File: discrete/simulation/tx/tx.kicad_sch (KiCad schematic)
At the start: 0 parts

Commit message: Add and validate discrete DEC logic level converter simulation
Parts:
- added D1: 1N914, Diode_THT:D_DO-35_SOD27_P7.62mm_Horizontal, symbol Diode:1N914
- added Q1: 2N3904, Package_TO_SOT_THT:TO-92_Inline, symbol Transistor_BJT:2N3904
- added Q2: 2N3906, Package_TO_SOT_THT:TO-92_Inline, symbol Transistor_BJT:2N3906
- added R1: 27k, symbol Device:R
- added R2: 180k, symbol Device:R
- added R3, R5: 100k, symbol Device:R
- added R4: 33k, symbol Device:R
- added R6: 10k, symbol Device:R
- added V1: 10, symbol Simulation_SPICE:VDC
- added V2: 15, symbol Simulation_SPICE:VDC
- added V3: VPULSE, symbol Simulation_SPICE:VPULSE
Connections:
- new net: Q2.2 (B), R4.2, R5.2
- new net: D1.1 (K), Q1.2 (B), R1.2, R2.2
- new net +10V: Q2.1 (E), R2.1, R3.1, R5.1, V1.1
- new net -15V: R6.2, V2.2
- new net DRV: Q2.3 (C), R6.1
- new net GND: D1.2 (A), Q1.1 (E), V1.2, V2.1, V3.2
- new net Q1_C: Q1.3 (C), R3.2, R4.1
- new net TTO: R1.1, V3.1

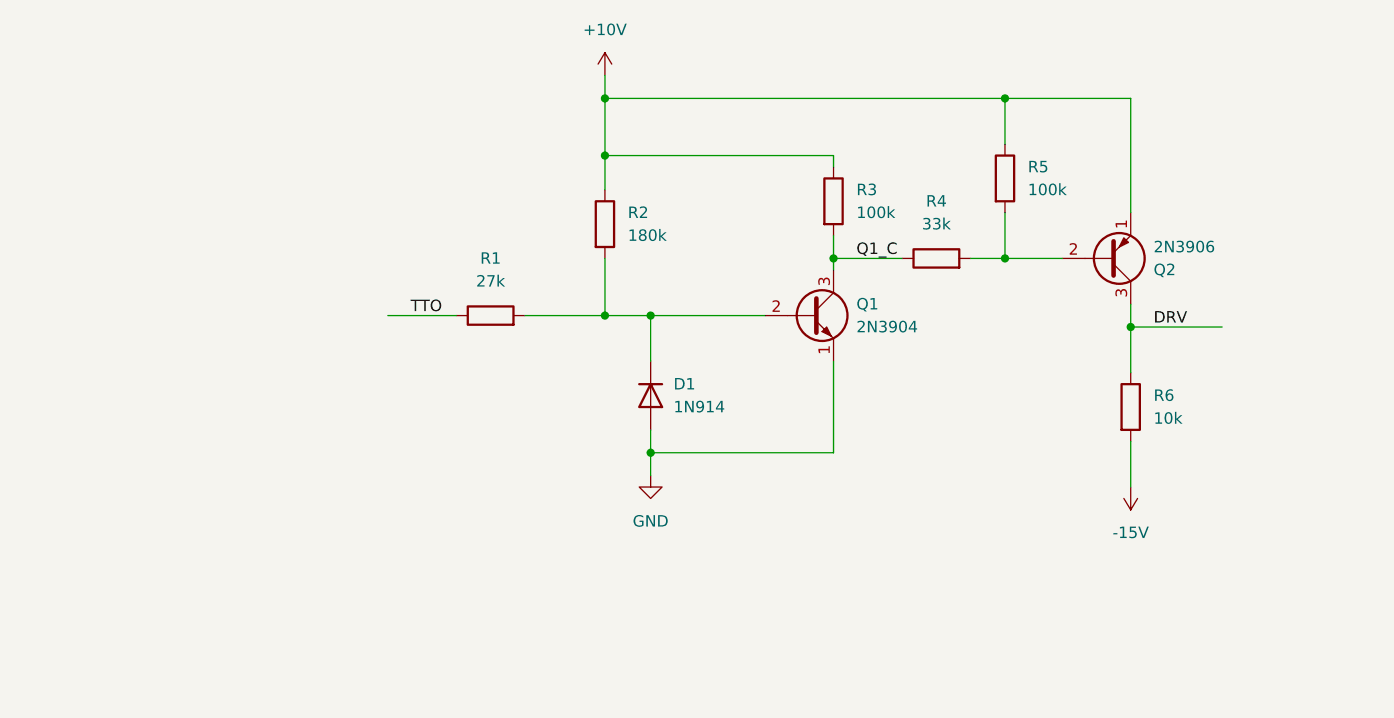
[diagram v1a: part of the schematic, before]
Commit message: Add and validate complementary RS232 transmitter output stage
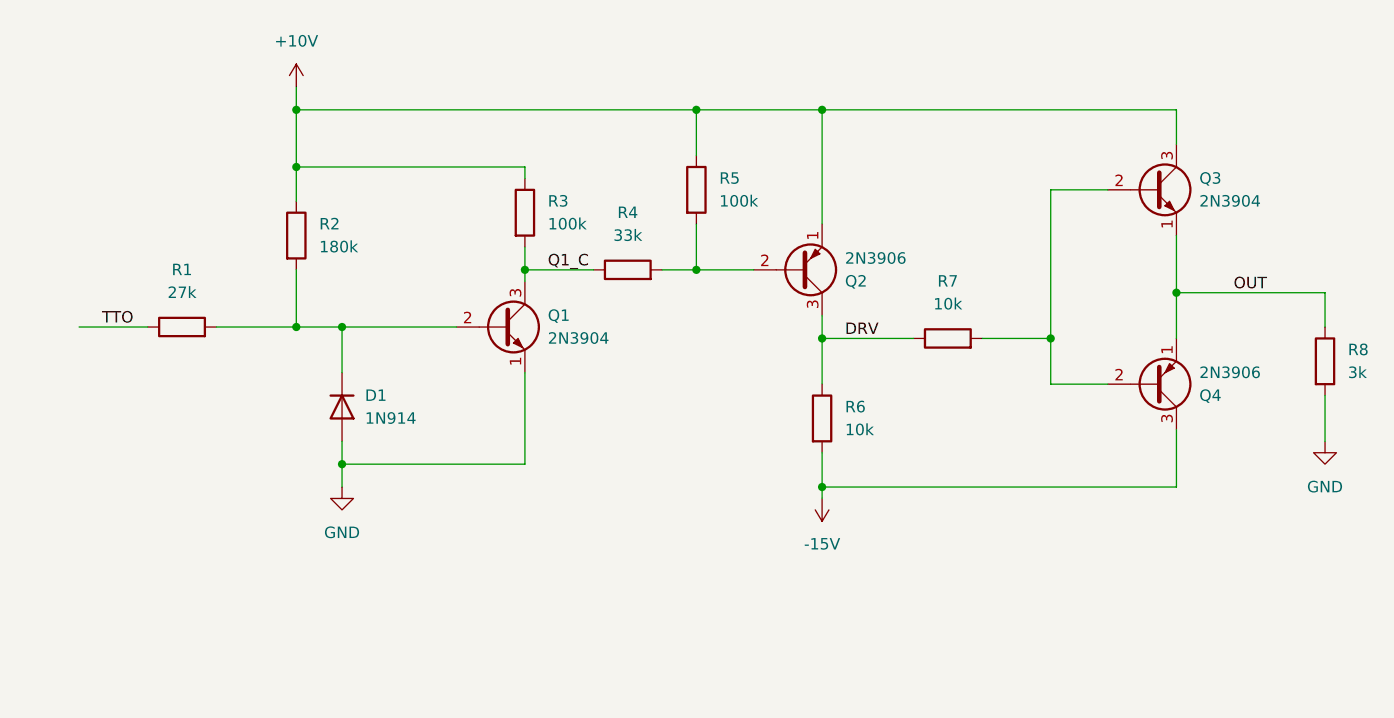
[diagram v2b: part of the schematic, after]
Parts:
- added Q3: 2N3904, Package_TO_SOT_THT:TO-92_Inline, symbol Transistor_BJT:2N3904
- added Q4: 2N3906, Package_TO_SOT_THT:TO-92_Inline, symbol Transistor_BJT:2N3906
- added R7: 10k, symbol Device:R
- added R8: 3k, symbol Device:R
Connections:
- net +10V: now also Q3.3 (C)
- net -15V: now also Q4.3 (C)
- net DRV: now also R7.1
- net GND: now also R8.2
- new net: Q3.2 (B), Q4.2 (B), R7.2
- new net OUT: Q3.1 (E), Q4.1 (E), R8.1
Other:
- moved on the sheet: D1, Q1, Q2, R1, R2, R3, R4, R5, R6

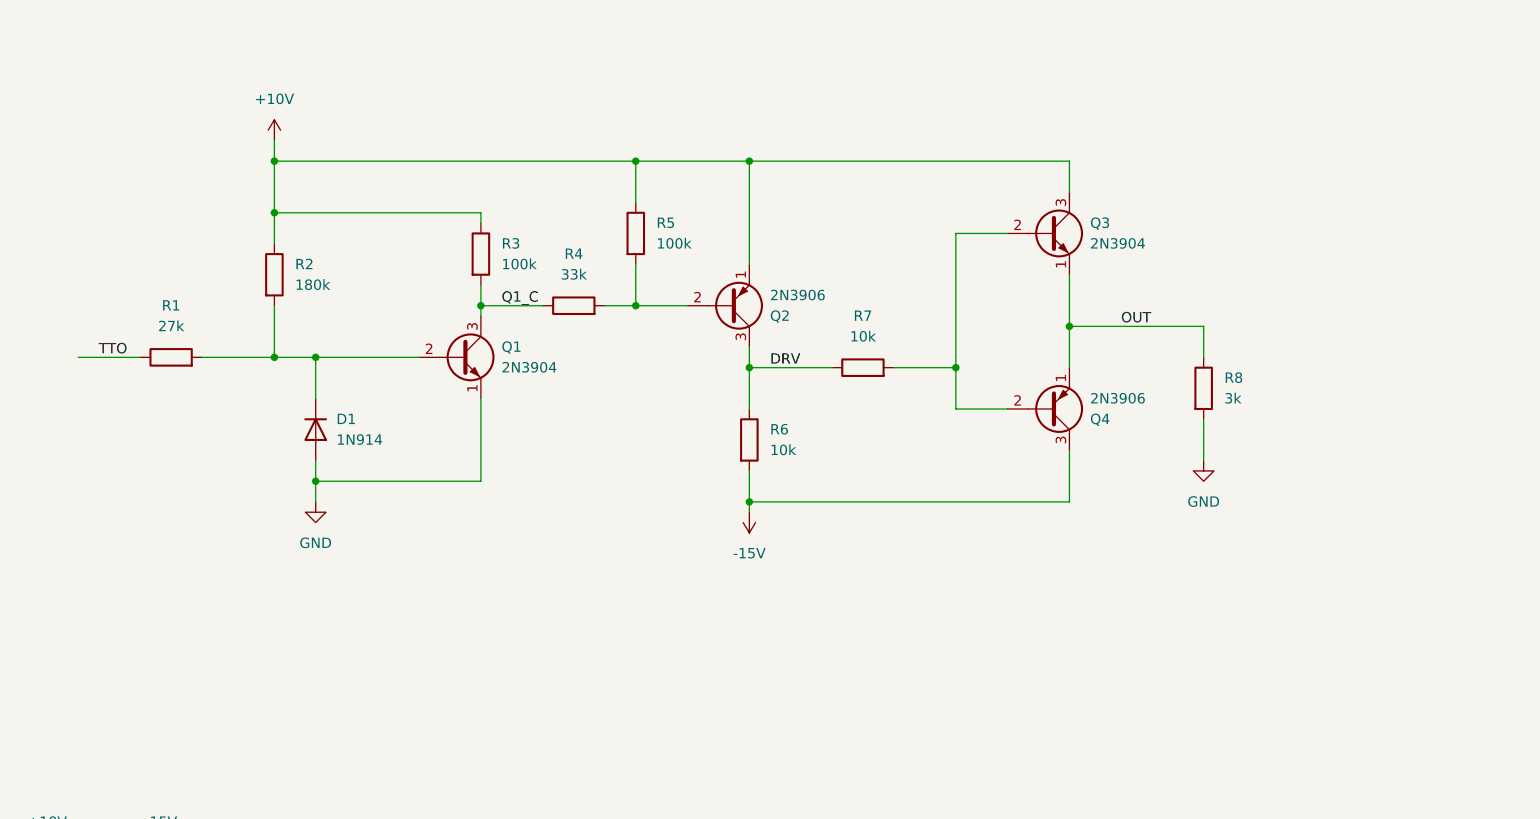
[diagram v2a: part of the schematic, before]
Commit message: Add RS232 transmitter normal load simulation
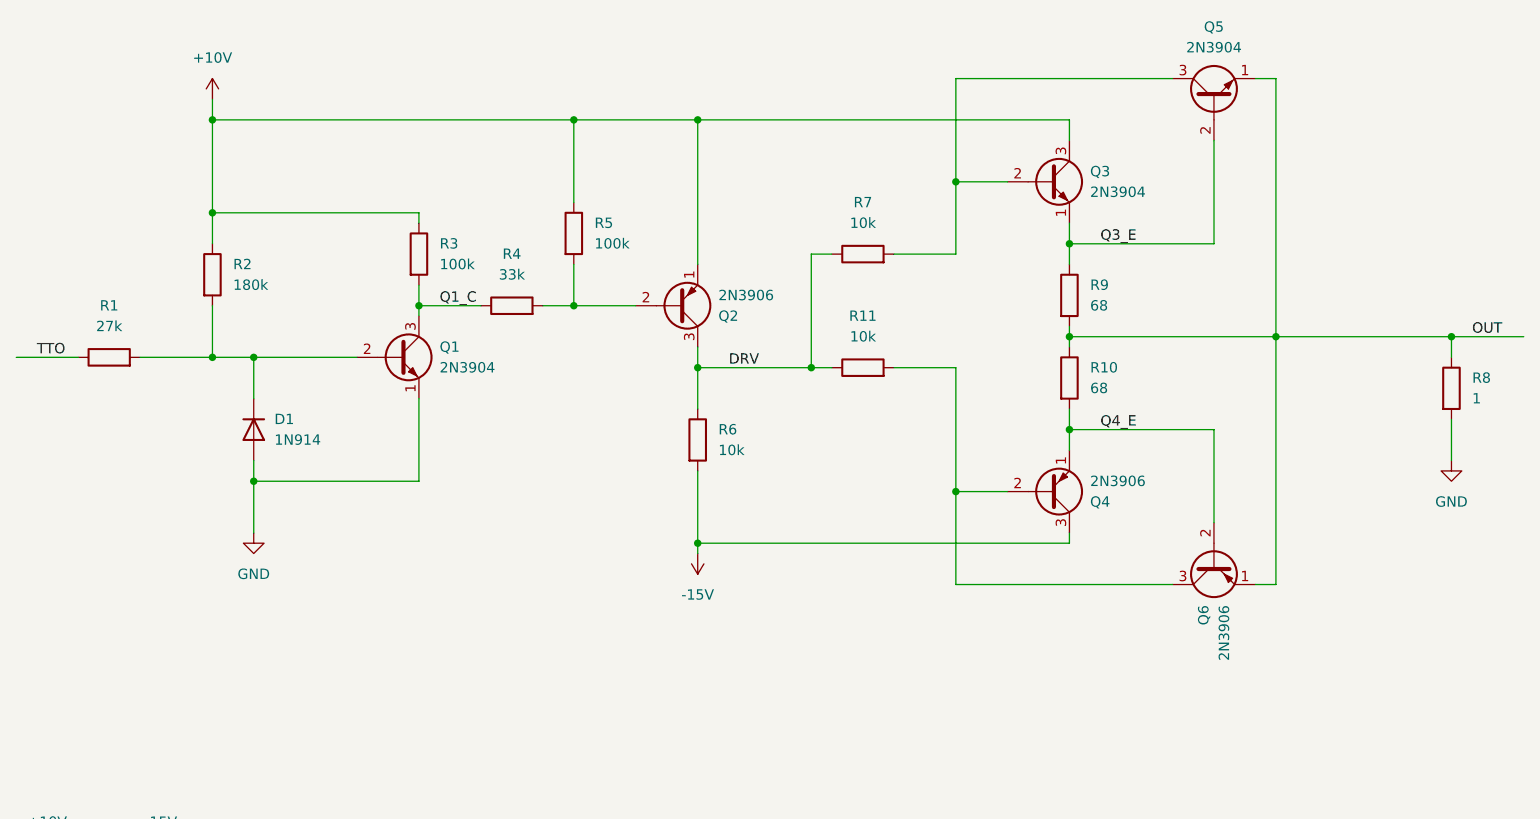
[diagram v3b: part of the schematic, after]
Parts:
- added Q5: 2N3904, Package_TO_SOT_THT:TO-92_Inline, symbol Transistor_BJT:2N3904
- added Q6: 2N3906, Package_TO_SOT_THT:TO-92_Inline, symbol Transistor_BJT:2N3906
- added R10, R9: 68, symbol Device:R
- added R7: 10k, symbol Device:R
- R8: value 3k -> 1
- renumbered R7 to R11
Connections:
- net DRV: now also R7.1
- net OUT: now also Q5.1 (E), Q6.1 (E), R10.1, R9.2; no longer Q3.1 (E), Q4.1 (E)
- net at Q4.2 (B), R11.2: now also Q6.3 (C); no longer Q3.2 (B)
- new net: Q3.2 (B), Q5.3 (C), R7.2
- new net Q3_E: Q3.1 (E), Q5.2 (B), R9.1
- new net Q4_E: Q4.1 (E), Q6.2 (B), R10.2
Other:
- moved on the sheet: D1, Q1, Q2, Q3, Q4, R1, R2, R3, R4, R5, R6, R8

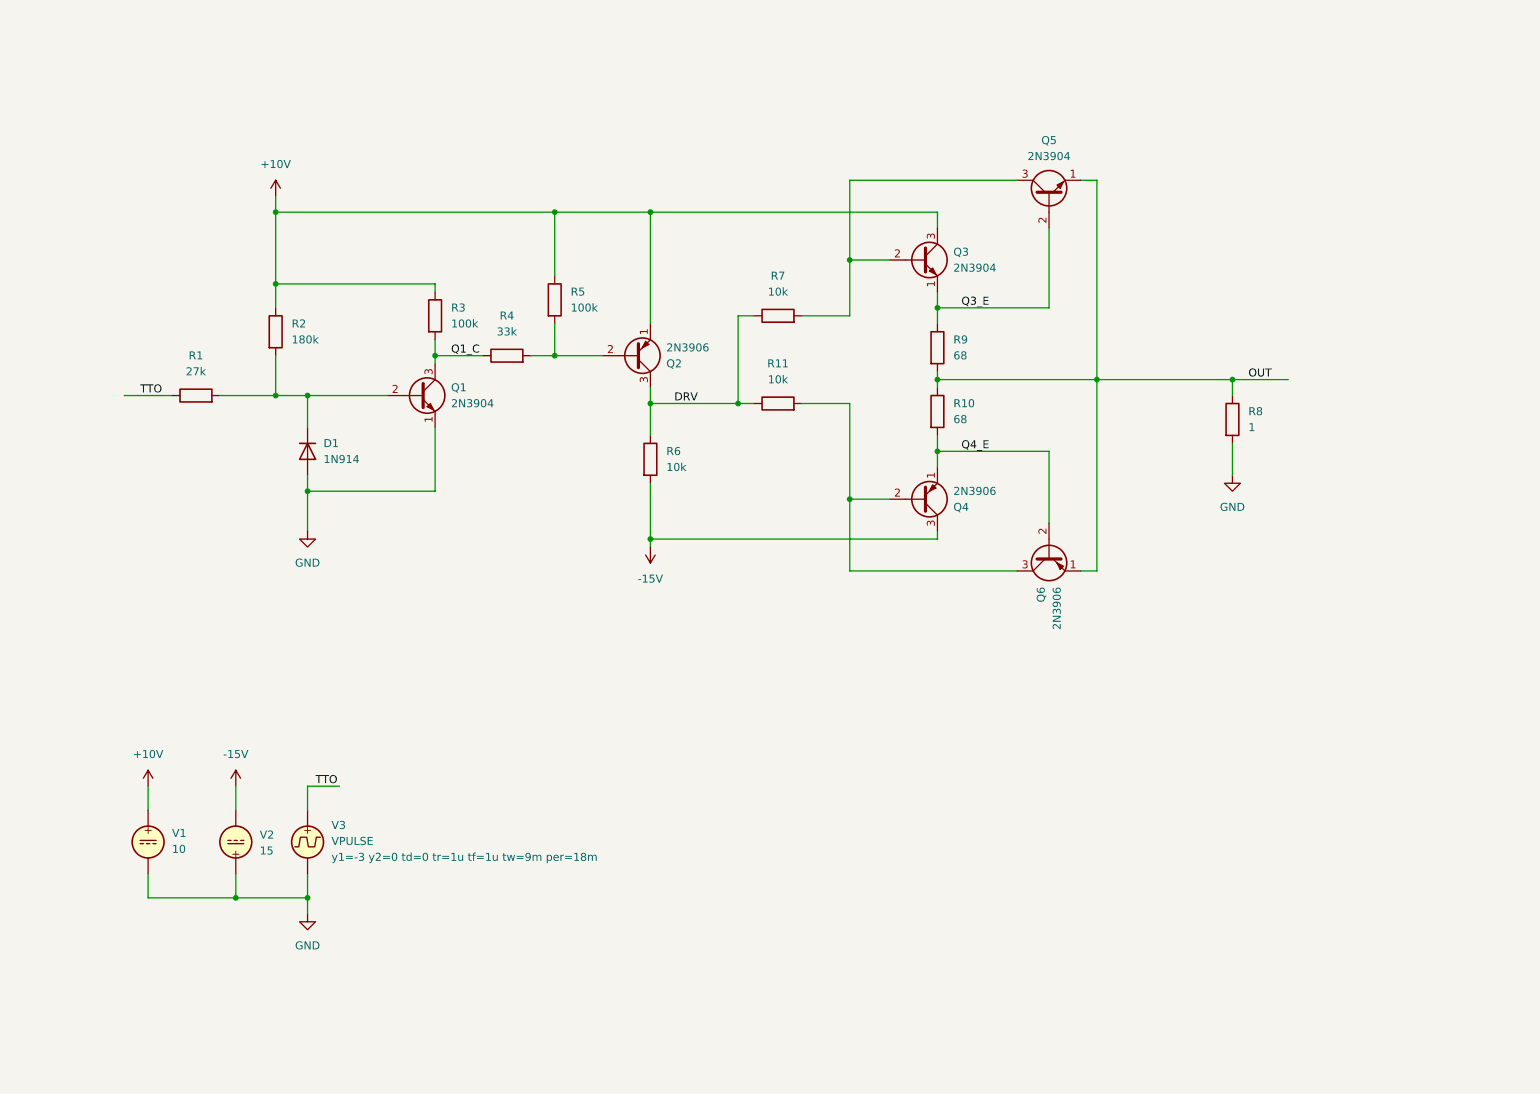
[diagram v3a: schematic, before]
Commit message: Add and validate RS232 transmitter fault protection
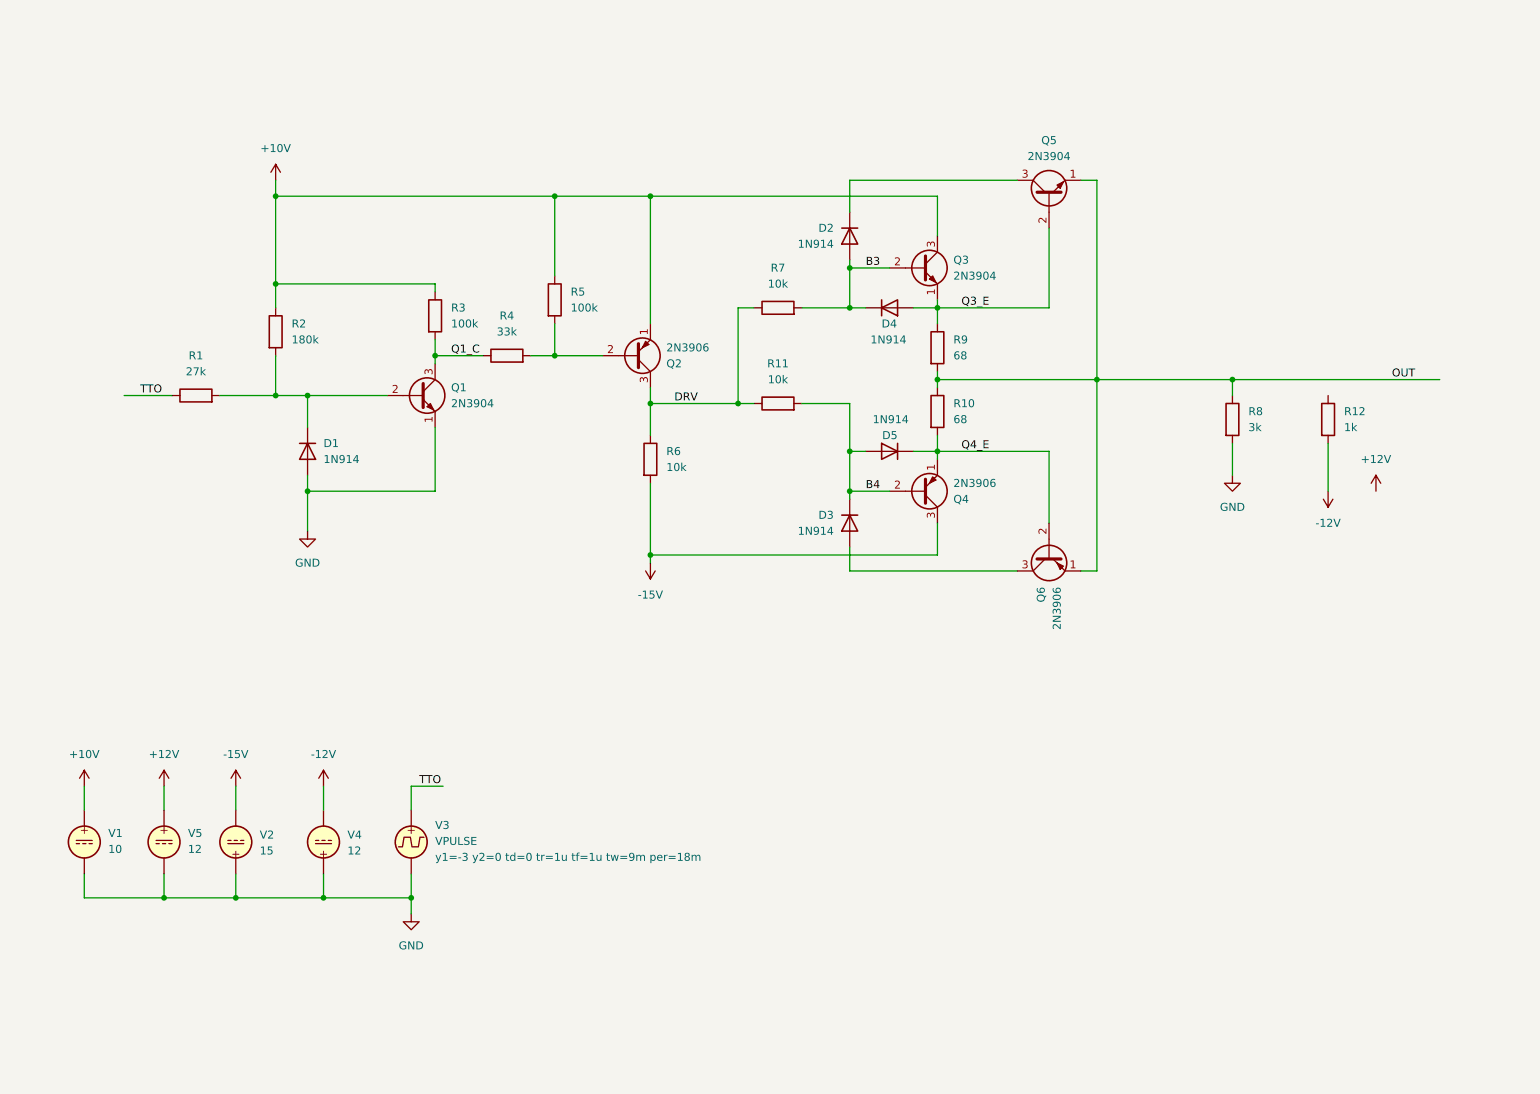
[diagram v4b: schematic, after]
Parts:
- added D2, D3, D4, D5: 1N914, Diode_THT:D_DO-35_SOD27_P7.62mm_Horizontal, symbol Diode:1N914
- added R12: 1k, symbol Device:R
- added V4, V5: 12, symbol Simulation_SPICE:VDC
- R8: value 1 -> 3k
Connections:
- net GND: now also V4.1, V5.2
- net Q3_E: now also D4.2 (A)
- net Q4_E: now also D5.1 (K)
- net B3: now reaches Q3.2 (B), R7.2
- net B3: now also D2.2 (A), D4.1 (K); no longer Q5.3 (C)
- net B4: now reaches Q4.2 (B), R11.2
- net B4: now also D3.1 (K), D5.2 (A); no longer Q6.3 (C)
- new net: D3.2 (A), Q6.3 (C)
- new net: D2.1 (K), Q5.3 (C)
- new net +12V: V5.1
- new net -12V: R12.2, V4.2
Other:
- moved on the sheet: Q3, Q4, R7, V1, V3
